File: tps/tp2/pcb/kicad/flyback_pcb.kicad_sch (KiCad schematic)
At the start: 37 parts, among them J1 Screw_Terminal_01x02, J2 Conn_01x11_Pin, J3 Conn_01x11_Pin, J4 Screw_Terminal_01x02, J5 Screw_Terminal_01x02, J6 Screw_Terminal_01x02, Q1 BUZ80, U1 UC3526N

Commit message: avances sch flyback + sch en pdf
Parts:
- removed C6, C9: 100u, symbol Device:C_Polarized
- removed C7: 1u, symbol Device:C
- removed R7, R8: 1400, Resistor_SMD:R_0805_2012Metric_Pad1.20x1.40mm_HandSolder, symbol Device:R
- added C14: 10n, symbol Device:C
- added C15: 2u-16V, symbol Device:C
- added C16: 10u-25V, symbol Device:C_Polarized
- added C17, C19: 1u-25V, symbol Device:C
- added C18: 100n-25V, symbol Device:C
- added C20: 5n-25V, symbol Device:C
- added JP2: Jumper_2_Open, TestPoint:TestPoint_2Pads_Pitch2.54mm_Drill0.8mm, symbol Jumper:Jumper_2_Open
- added JP3, JP4: Jumper_2_Open, symbol Jumper:Jumper_2_Open
- added R10: 130k, Resistor_THT:R_Axial_DIN0411_L9.9mm_D3.6mm_P12.70mm_Horizontal, symbol Device:R
- added R11: 24k, Resistor_THT:R_Axial_DIN0411_L9.9mm_D3.6mm_P12.70mm_Horizontal, symbol Device:R
- added R12, R13: 10k, Resistor_THT:R_Axial_DIN0411_L9.9mm_D3.6mm_P12.70mm_Horizontal, symbol Device:R
- added R14: 4.7k, Resistor_THT:R_Axial_DIN0411_L9.9mm_D3.6mm_P12.70mm_Horizontal, symbol Device:R
- added R9: 120, Resistor_THT:R_Axial_DIN0411_L9.9mm_D3.6mm_P12.70mm_Horizontal, symbol Device:R
- added RD: 0, Resistor_THT:R_Axial_DIN0411_L9.9mm_D3.6mm_P12.70mm_Horizontal, symbol Device:R
- added RT: 3.3k, Resistor_THT:R_Axial_DIN0411_L9.9mm_D3.6mm_P12.70mm_Horizontal, symbol Device:R
- added RV1: 20k, Potentiometer_THT:Potentiometer_Bourns_3266Y_Vertical, symbol Device:R_Potentiometer_Trim
- added RV2: 100k, Potentiometer_THT:Potentiometer_Bourns_3266Y_Vertical, symbol Device:R_Potentiometer_Trim
- C1, C2: value 100u -> 100u-600V
- C10: value 100u -> 47u-35V
- C11: value 1u -> 100n-35V
- C12: value 1u -> 1u-35V
- C13: value C -> 2.6n-600V
- C3, C4: value 1u -> 1u-600V
- C5: value 100u -> 47u-25V
- C8: value 1u -> 100n-25V
- D1: value RB157 -> W10M
- J1, J4, J5, J6: value Screw_Terminal_01x02 -> Bornera
- R3: value 301 -> 330-1/4W
- R4: value 1400 -> 1.5k-1/4W
- R5: value 80 -> 51k
- R6: value 31k -> 68k-2W
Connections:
- net +16V: now also C16.1, C17.1, C18.1, R10.1
- net +5V: now also C19.1
- net GND1: now also R4.2, C14.2, C15.2, C16.2, C17.2, C18.2, C20.2, JP3.2 (B), JP4.2 (B), R11.2, R13.2, RD.1, RT.1, RV1.3, RV2.3
- net GND2: now also C19.2; no longer R4.2
- net ERROR+: now reaches U1.1 (+ERROR)
- net ERROR+: now also R12.2, R13.1, RV1.1, RV1.2
- net at U1.10 (CT): now also C20.1
- net at U1.11 (RD): now also RD.2
- net VREF: now reaches U1.18 (VREF)
- net VREF: now also R12.1
- net ERROR-: now reaches U1.2 (-ERROR)
- net ERROR-: now also R10.2, R11.1
- net COMP: now reaches U1.3 (COMP)
- net COMP: now also JP2.2 (B), R14.1
- net SOFTSTART: now reaches U1.4 (CSS)
- net SOFTSTART: now also C15.1
- net nRESET: now reaches U1.5 (RESET*)
- net nRESET: now also JP4.1 (A)
- net nSHUTDOWN: now reaches U1.8 (SHUTDOWN*)
- net nSHUTDOWN: now also JP3.1 (A)
- net at U1.9 (RTIMING): now also RT.2
- net at C13.2, R5.2: now also R9.1; no longer D6.1 (K)
- new net: C14.1, R14.2
- new net: JP2.1 (A), RV2.1, RV2.2
- new net: D6.1 (K), R9.2
- no-connect marks 1 -> 4
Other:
- note added: "(100uA x 100ms)/5V"
- note added: "(311V-2V)/5mA"
- note added: "1000V-1.5A"
- note added: "2.5V"
- note added: "5V"
- note added: "Ajuste de la referencia"
- note added: "Control manual de COMP"
- note added: "Desacople del IC"
- note added: "Feedback"
- note added: "Pulling nSHUTDOWN LOW immediately inhibits all PWM output pulses. Holding nRESET LOW discharges the soft-start capacitor."
- note added: "RT <- 3.3k CT <- 5nF RD <- 0 (default deadtime) Oscillator Period <- 8uS Fosc <- 125kHz"
- note added: "Snubber"
- note added: "Trafo"
- note removed: "(311V-2V)/10mA"
- company: (none) -> 22.28 - Electrónica de Potencia
- title: (none) -> TP2 - Convertidor Flyback
- moved on the sheet: C1, C10, C11, C13, C2, C3, C4, C5, C8, D1, D2, D3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

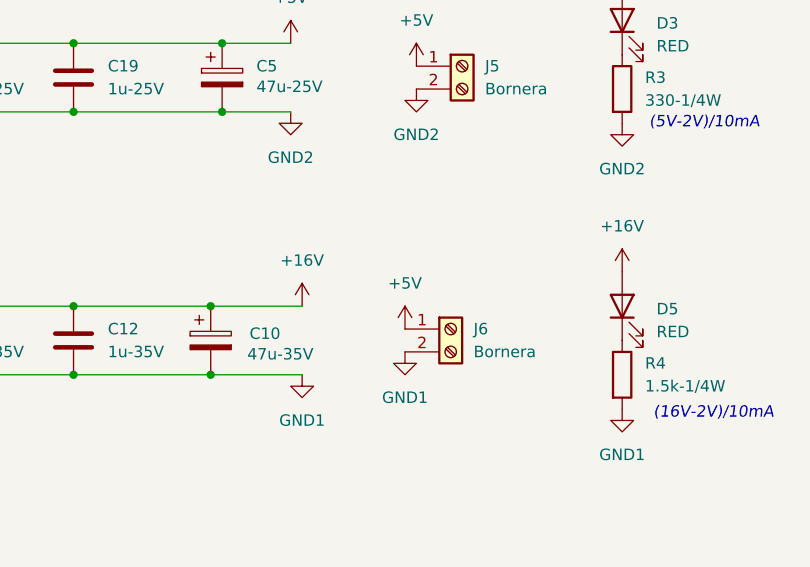
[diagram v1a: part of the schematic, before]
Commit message: fix nodo alimentación bornera J6
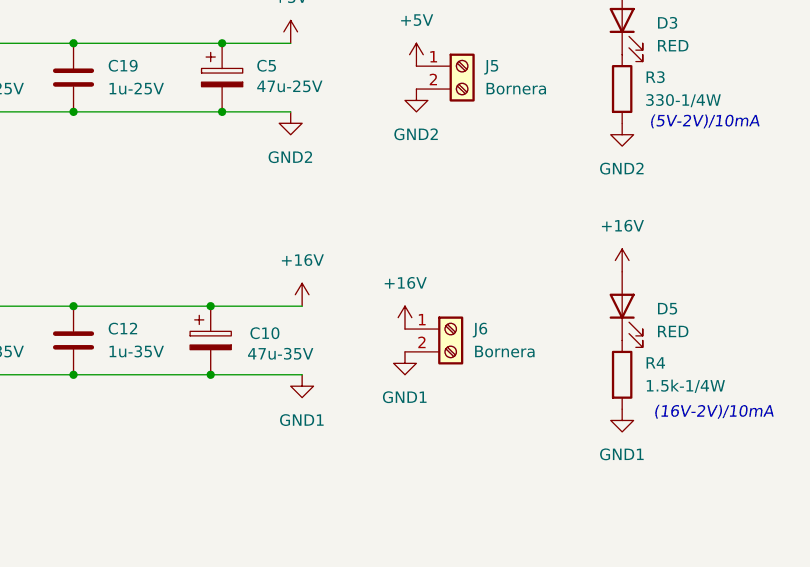
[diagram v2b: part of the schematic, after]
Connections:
- net +16V: now also J6.1 (Pin_1)
- net +5V: no longer J6.1 (Pin_1)
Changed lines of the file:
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@@
+	)
+	(symbol
+		(lib_id "power:+12V")
+		(at 91.44 91.44 0)
+		(unit 1)
+		(exclude_from_sim no)
+		(in_bom yes)
+		(on_board yes)
+		(dnp no)
+		(fields_autoplaced yes)
+		(property "Reference" "#PWR045"
+			(at 91.44 95.25 0)
+			(effects
+				(font
+					(size 1.27 1.27)
+				)
+				(hide yes)
+			)
+		)
+		(property "Value" "+16V"
+			(at 91.44 86.36 0)
+			(effects
+				(font
+					(size 1.27 1.27)
+				)
+			)
+		)
+		(property "Footprint" ""
+			(at 91.44 91.44 0)
+			(effects
+				(font
+					(size 1.27 1.27)
+				)
+				(hide yes)
+			)
+		)
+		(property "Datasheet" ""
+			(at 91.44 91.44 0)
+			(effects
+				(font
+					(size 1.27 1.27)
+				)
+				(hide yes)
+			)
+		)
+		(property "Description" "Power symbol creates a global label with name \"+12V\""
+			(at 91.44 91.44 0)
+			(effects
+				(font
+					(size 1.27 1.27)
+				)
+				(hide yes)
+			)
+		)
+		(pin "1"
+		)
+		(instances
+			(project "flyback_pcb"
+				(path "/847a25f2-0901-4b4c-9f93-5b1d0db6f010"
+					(reference "#PWR045")
+					(unit 1)
+				)
+			)
+		)
 	)
 	(symbol
@@
 					(unit 1)
 				)
-			)
-		)
-	)
-	(symbol
-		(lib_id "power:+12V")
-		(at 91.44 91.44 0)
-		(unit 1)
-		(exclude_from_sim no)
-		(in_bom yes)
-		(on_board yes)
-		(dnp no)
-		(fields_autoplaced yes)
-		(property "Reference" "#PWR023"
-			(at 91.44 95.25 0)
-			(effects
-				(font
-					(size 1.27 1.27)
-				)
-				(hide yes)
-			)
-		)
-		(property "Value" "+5V"
-			(at 91.44 86.36 0)
-			(effects
-				(font
-					(size 1.27 1.27)
-				)
-			)
-		)
-		(property "Footprint" ""
-			(at 91.44 91.44 0)
-			(effects
-				(font
-					(size 1.27 1.27)
-				)
-				(hide yes)
-			)
-		)
-		(property "Datasheet" ""
-			(at 91.44 91.44 0)
-			(effects
-				(font
-					(size 1.27 1.27)
-				)
-				(hide yes)
-			)
-		)
-		(property "Description" "Power symbol creates a global label with name \"+12V\""
-			(at 91.44 91.44 0)
-			(effects
-				(font
-					(size 1.27 1.27)
-				)
-				(hide yes)
-			)
-		)
-		(pin "1"
-		)
-		(instances
-			(project "flyback_pcb"
-				(path "/847a25f2-0901-4b4c-9f93-5b1d0db6f010"
-					(reference "#PWR023")
-					(unit 1)
-				)

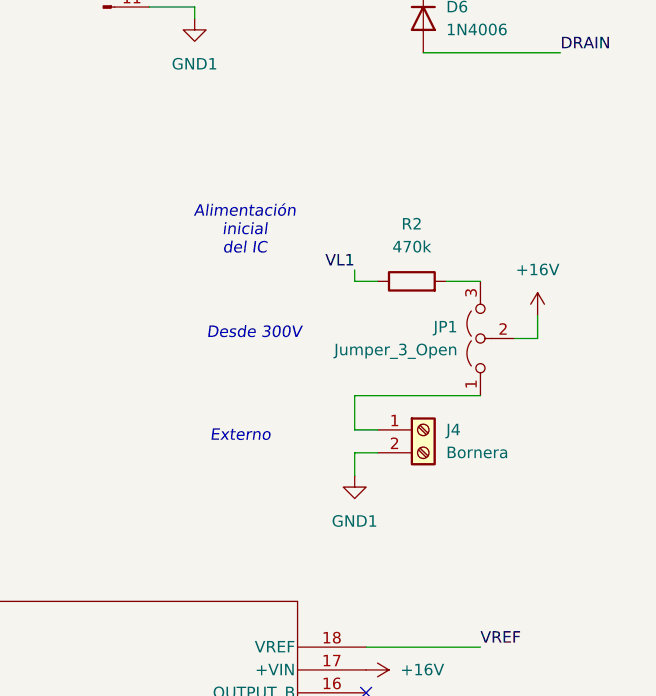
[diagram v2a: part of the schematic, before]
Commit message: agrego diodo en serie a la alimentación externa del IC
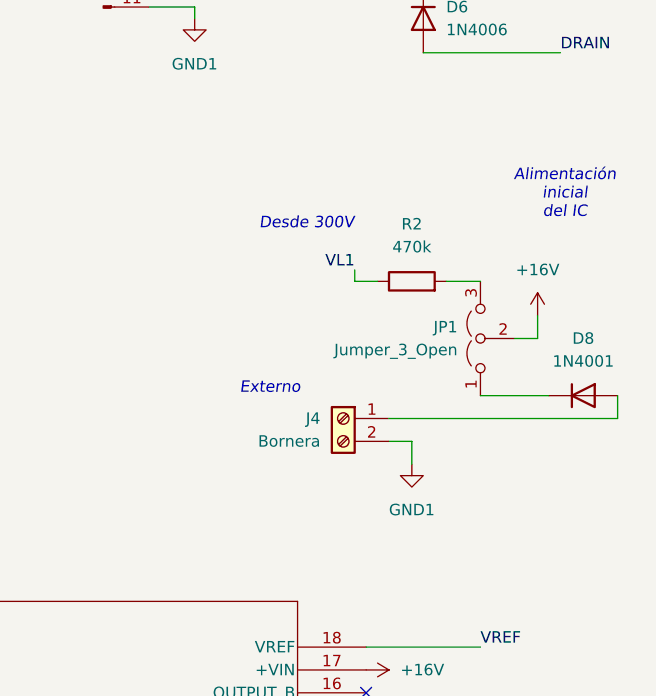
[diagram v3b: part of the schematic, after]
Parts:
- added D8: 1N4001, Diode_THT:D_DO-41_SOD81_P10.16mm_Horizontal, symbol Diode:1N4001
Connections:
- net at J4.1 (Pin_1): now also D8.2 (A); no longer JP1.1 (A)
- new net: D8.1 (K), JP1.1 (A)
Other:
- moved on the sheet: J4
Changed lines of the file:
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@@
 	(text "Desde 300V"
 		(exclude_from_sim no)
-		(at 237.744 83.312 0)
+		(at 243.586 71.12 0)
 		(effects
 			(font
@@
 	(text "Alimentación\ninicial\ndel IC"
 		(exclude_from_sim no)
-		(at 236.728 71.882 0)
+		(at 272.288 67.818 0)
 		(effects
 			(font
@@
 	(text "Externo"
 		(exclude_from_sim no)
-		(at 236.22 94.742 0)
+		(at 239.522 89.408 0)
 		(effects
 			(font
@@
 	(wire
 		(pts
-			(xy 248.92 90.17) (xy 248.92 93.98)
-		)
-		(stroke
-			(width 0)
-			(type default)
-		)
-	)
-	(wire
-		(pts
 			(xy 35.56 88.9) (xy 36.83 88.9)
 		)
@@
 	(wire
 		(pts
-			(xy 248.92 96.52) (xy 248.92 99.06)
+			(xy 255.27 95.25) (xy 255.27 97.79)
 		)
 		(stroke
@@
 	(wire
 		(pts
-			(xy 251.46 93.98) (xy 248.92 93.98)
+			(xy 252.73 92.71) (xy 278.13 92.71)
 		)
 		(stroke
@@
 	(wire
 		(pts
+			(xy 262.89 90.17) (xy 270.51 90.17)
+		)
+		(stroke
+			(width 0)
+			(type default)
+		)
+	)
+	(wire
+		(pts
 			(xy 35.56 59.69) (xy 36.83 59.69)
 		)
@@
 	(wire
 		(pts
-			(xy 262.89 90.17) (xy 248.92 90.17)
-		)
-		(stroke
-			(width 0)
-			(type default)
-		)
-	)
-	(wire
-		(pts
 			(xy 146.05 135.89) (xy 158.75 135.89)
 		)
@@
 	(wire
 		(pts
-			(xy 251.46 96.52) (xy 248.92 96.52)
+			(xy 252.73 95.25) (xy 255.27 95.25)
 		)
 		(stroke
@@
 	(wire
 		(pts
+			(xy 278.13 90.17) (xy 278.13 92.71)
+		)
+		(stroke
+			(width 0)
+			(type default)
+		)
+	)
+	(wire
+		(pts
 			(xy 54.61 59.69) (xy 71.12 59.69)
 		)
@@
 	(symbol
 		(lib_id "Connector:Screw_Terminal_01x02")
-		(at 256.54 93.98 0)
+		(at 247.65 92.71 0)
+		(mirror y)
 		(unit 1)
 		(exclude_from_sim no)
@@
 		(fields_autoplaced yes)
 		(property "Reference" "J4"
-			(at 259.08 93.9799 0)
+			(at 245.11 92.7099 0)
 			(effects
 				(font
@@
 		)
 		(property "Value" "Bornera"
-			(at 259.08 96.5199 0)
+			(at 245.11 95.2499 0)
 			(effects
 				(font
@@
 		)
 		(property "Footprint" ""
-			(at 256.54 93.98 0)
+			(at 247.65 92.71 0)
 			(effects
 				(font
@@
 		)
 		(property "Datasheet" "~"
-			(at 256.54 93.98 0)
+			(at 247.65 92.71 0)
 			(effects
 				(font
@@
 		)
 		(property "Description" "Generic screw terminal, single row, 01x02, script generated (kicad-library-utils/schlib/autogen/connector/)"
-			(at 256.54 93.98 0)
+			(at 247.65 92.71 0)
 			(effects
 				(font
@@
 	(symbol
 		(lib_id "power:GND1")
-		(at 248.92 99.06 0)
+		(at 255.27 97.79 0)
+		(mirror y)
 		(unit 1)
 		(exclude_from_sim no)
@@
 		(fields_autoplaced yes)
 		(property "Reference" "#PWR014"
-			(at 248.92 105.41 0)
+			(at 255.27 104.14 0)
 			(effects
 				(font
@@
 		)
 		(property "Value" "GND1"
-			(at 248.92 104.14 0)
+			(at 255.27 102.87 0)
 			(effects
 				(font
@@
 		)
 		(property "Footprint" ""
-			(at 248.92 99.06 0)
+			(at 255.27 97.79 0)
 			(effects
 				(font
@@
 		)
 		(property "Datasheet" ""
-			(at 248.92 99.06 0)
+			(at 255.27 97.79 0)
 			(effects
 				(font
@@
 		)
 		(property "Description" "Power symbol creates a global label with name \"GND1\" , ground"
-			(at 248.92 99.06 0)
+			(at 255.27 97.79 0)
 			(effects
 				(font
@@
 	)
 	(symbol
+		(lib_id "Diode:1N4001")
+		(at 274.32 90.17 0)
+		(unit 1)
+		(exclude_from_sim no)
+		(in_bom yes)
+		(on_board yes)
+		(dnp no)
+		(fields_autoplaced yes)
+		(property "Reference" "D8"
+			(at 274.32 83.82 0)
+			(effects
+				(font
+					(size 1.27 1.27)
+				)
+			)
+		)
+		(property "Value" "1N4001"
+			(at 274.32 86.36 0)
+			(effects
+				(font
+					(size 1.27 1.27)
+				)
+			)
+		)
+		(property "Footprint" "Diode_THT:D_DO-41_SOD81_P10.16mm_Horizontal"
+			(at 274.32 90.17 0)
+			(effects
+				(font
+					(size 1.27 1.27)
+				)
+				(hide yes)
+			)
+		)
+		(property "Datasheet" "http://www.vishay.com/docs/88503/1n4001.pdf"
+			(at 274.32 90.17 0)
+			(effects
+				(font
+					(size 1.27 1.27)
+				)
+				(hide yes)
+			)
+		)
+		(property "Description" "50V 1A General Purpose Rectifier Diode, DO-41"
+			(at 274.32 90.17 0)
+			(effects
+				(font
+					(size 1.27 1.27)
+				)
+				(hide yes)
+			)
+		)
+		(property "Sim.Device" "D"
+			(at 274.32 90.17 0)
+			(effects
+				(font
+					(size 1.27 1.27)
+				)
+				(hide yes)
+			)
+		)
+		(property "Sim.Pins" "1=K 2=A"
+			(at 274.32 90.17 0)
+			(effects
+				(font
+					(size 1.27 1.27)
+				)
+				(hide yes)
+			)
+		)
+		(pin "2"
+		)
+		(pin "1"
+		)
+		(instances
+			(project "flyback_pcb"
+				(path "/847a25f2-0901-4b4c-9f93-5b1d0db6f010"
+					(reference "D8")
+					(unit 1)
+				)
+			)
+		)
+	)
+	(symbol
 		(lib_id "Device:C_Polarized")
 		(at 71.12 63.5 0)
@@
 		(at 134.62 171.45 270)
 		(unit 1)
-		(exclude_from_sim yes)
+		(exclude_from_sim no)
 		(in_bom yes)
 		(on_board yes)
@@
 		(at 156.21 171.45 270)
 		(unit 1)
-		(exclude_from_sim yes)
+		(exclude_from_sim no)
 		(in_bom yes)
 		(on_board yes)

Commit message: add cap footprints
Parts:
- removed C11: 100n-35V, symbol Device:C
- removed C2: 100u-600V, symbol Device:C_Polarized
- removed C3: 1u-600V, symbol Device:C
- removed C8: 100n-25V, symbol Device:C
- C1: renamed from C13; footprint (none) -> Capacitor_THT:C_Disc_D4.3mm_W1.9mm_P5.00mm
- C10, C5: footprint (none) -> Capacitor_THT:CP_Radial_D14.0mm_P5.00mm
- C11: renamed from C20; footprint (none) -> Capacitor_THT:C_Disc_D4.3mm_W1.9mm_P5.00mm
- C12: renamed from C15; footprint (none) -> Capacitor_THT:C_Disc_D4.3mm_W1.9mm_P5.00mm
- C13: renamed from C14; footprint (none) -> Capacitor_THT:C_Disc_D4.3mm_W1.9mm_P5.00mm
- C2: renamed from C1; footprint (none) -> Capacitor_THT:CP_Radial_D14.0mm_P5.00mm
- C4: renamed from C19; footprint (none) -> Capacitor_THT:C_Disc_D4.3mm_W1.9mm_P5.00mm
- C6: renamed from C16; footprint (none) -> Capacitor_THT:CP_Radial_D14.0mm_P5.00mm
- C7: renamed from C17; footprint (none) -> Capacitor_THT:C_Disc_D4.3mm_W1.9mm_P5.00mm
- C8: renamed from C18; footprint (none) -> Capacitor_THT:C_Disc_D4.3mm_W1.9mm_P5.00mm
- C9: renamed from C12; footprint (none) -> Capacitor_THT:C_Disc_D4.3mm_W1.9mm_P5.00mm
- renumbered C4 to C3, D7 to D1, D1 to D2, D6 to D3, D3 to D4, D2 to D5, D4 to D6, D5 to D7, J5 to J4, J6 to J5, J4 to J6, R5 to R1, R11 to R10, R13 to R11, R14 to R12, R6 to R2, R9 to R3, R1 to R4, R3 to R5, R2 to R6, R4 to R7, R10 to R8, R12 to R9, RD to RD1, RT to RT1
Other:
- moved on the sheet: C10, C3, C4, C5, C9

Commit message: add missing footprints
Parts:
- C3: footprint (none) -> Capacitor_THT:C_Disc_D4.3mm_W1.9mm_P5.00mm
- J1, J4, J5, J6: footprint (none) -> TerminalBlock:TerminalBlock_bornier-2_P5.08mm
- JP1: footprint (none) -> Connector_PinHeader_2.54mm:PinHeader_1x03_P2.54mm_Vertical
- JP3, JP4: footprint (none) -> Connector_PinHeader_2.54mm:PinHeader_1x02_P2.54mm_Vertical
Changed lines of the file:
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@@
 			)
 		)
-		(property "Footprint" ""
+		(property "Footprint" "TerminalBlock:TerminalBlock_bornier-2_P5.08mm"
 			(at 31.75 29.21 0)
 			(effects
@@
 			)
 		)
-		(property "Footprint" ""
+		(property "Footprint" "TerminalBlock:TerminalBlock_bornier-2_P5.08mm"
 			(at 96.52 91.44 0)
 			(effects
@@
 			)
 		)
-		(property "Footprint" ""
+		(property "Footprint" "TerminalBlock:TerminalBlock_bornier-2_P5.08mm"
 			(at 247.65 92.71 0)
 			(effects
@@
 			)
 		)
-		(property "Footprint" ""
+		(property "Footprint" "TerminalBlock:TerminalBlock_bornier-2_P5.08mm"
 			(at 97.79 62.23 0)
 			(effects
@@
 			)
 		)
-		(property "Footprint" ""
+		(property "Footprint" "Connector_PinHeader_2.54mm:PinHeader_1x03_P2.54mm_Vertical"
 			(at 262.89 83.82 0)
 			(effects
@@
 			)
 		)
-		(property "Footprint" ""
+		(property "Footprint" "Connector_PinHeader_2.54mm:PinHeader_1x02_P2.54mm_Vertical"
 			(at 134.62 171.45 0)
 			(effects
@@
 			)
 		)
-		(property "Footprint" ""
+		(property "Footprint" "Capacitor_THT:C_Disc_D4.3mm_W1.9mm_P5.00mm"
 			(at 106.3752 34.29 0)
 			(effects
@@
 			)
 		)
-		(property "Footprint" ""
+		(property "Footprint" "Connector_PinHeader_2.54mm:PinHeader_1x02_P2.54mm_Vertical"
 			(at 156.21 171.45 0)
 			(effects
